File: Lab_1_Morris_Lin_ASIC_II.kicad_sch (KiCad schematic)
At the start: 100 parts, among them IC1 74CBTLV3253D,118, IC2 74CBTLV3253D,118, IC3 74CBTLV3253D,118, IC4 74CBTLV3253D,118, IC5 74CBTLV3253D,118, IC6 74CBTLV3253D,118, J1 VDDPST_External, J10 Conn_01x14, J11 Conn_01x14, J2 PMOD_A, J3 PMOD_B, J4 VDD_Qn External, J5 VDDPST External, J6 PMOD_A, J7 PMOD_B, J8 Conn_01x14, J9 Conn_01x14, Q1 BSS138, U1 TLV75710PDBV, U2 TLV75710PDBV

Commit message: Routing Attempt 2 initial
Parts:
- removed D7: ~{OE}, LED_SMD:LED_1206_3216Metric_Pad1.42x1.75mm_HandSolder, symbol Device:LED
- removed J1: VDDPST_External, Connector:Banana_Jack_2Pin, symbol Connector_Generic:Conn_01x02
- removed R8: 470, Resistor_SMD:R_1206_3216Metric_Pad1.30x1.75mm_HandSolder, symbol Device:R_US
- added J12: VDDPST External, Connector:Banana_Jack_2Pin, symbol Connector_Generic:Conn_01x02
- H1, H2, H3, H4: symbol Mechanical:MountingHole -> Mechanical:MountingHole_Pad
- J2, J3: now in the parts list
- J5: value VDDPST External -> VDDRING External
- J6: value PMOD_A -> Logic_Analyzer_PMOD_A; footprint ASIC_II:PinHeader_VertNum_2x06_P2.54mm_Vertical -> ASIC_II:PinHeader_VertNum_2x05_P2.54mm_Vertical; symbol Connector_Generic:Conn_02x06_Top_Bottom -> Connector_Generic:Conn_02x05_Top_Bottom; now in the parts list
- J7: value PMOD_B -> Logic_Analyzer_PMOD_B; footprint ASIC_II:PinHeader_VertNum_2x06_P2.54mm_Vertical -> ASIC_II:PinHeader_VertNum_2x05_P2.54mm_Vertical; symbol Connector_Generic:Conn_02x06_Top_Bottom -> Connector_Generic:Conn_02x05_Top_Bottom; now in the parts list
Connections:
- net GND: now also J6.10 (Pin_10), J6.5 (Pin_5), J7.10 (Pin_10), J7.5 (Pin_5), J12.2 (Pin_2); no longer J6.12 (Pin_12), J6.6 (Pin_6), J7.12 (Pin_12), J7.6 (Pin_6), JP5.3 (B), JP6.3 (B), JP9.3 (B)
- net PMOD_A10: now also J6.9 (Pin_9); no longer J6.10 (Pin_10)
- net PMOD_A7: now also J6.6 (Pin_6); no longer J6.7 (Pin_7)
- net PMOD_A8: now also J6.7 (Pin_7); no longer J6.8 (Pin_8)
- net PMOD_A9: now also J6.8 (Pin_8); no longer J6.9 (Pin_9)
- net PMOD_B10: now also J7.9 (Pin_9), JP6.3 (B); no longer J7.10 (Pin_10)
- net PMOD_B7: now also J7.6 (Pin_6); no longer J7.7 (Pin_7)
- net PMOD_B8: now also J7.7 (Pin_7), JP5.3 (B); no longer J7.8 (Pin_8)
- net PMOD_B9: now also J7.8 (Pin_8), JP9.3 (B); no longer J7.9 (Pin_9)
- net at JP1.3 (B): now also J12.1 (Pin_1)
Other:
- note removed: "Output Disabled LED"
- moved on the sheet: C6, J10, R10, R5, R6

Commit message: Preroute self planned
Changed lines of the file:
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@@
 		)
 	)
-	(text "Select Lines and ~{OE}\nIndicator LEDs"
+	(text "Select Lines and ~{OE} Indicator LEDs"
 		(exclude_from_sim no)
 		(at 17.78 214.63 0)
@@
 		)
 	)
-	(netclass_flag ""
-		(length 2.54)
-		(shape round)
-		(at 44.45 115.57 0)
-		(fields_autoplaced yes)
-		(effects
-			(font
-				(size 1.27 1.27)
+	(rule_area
+		(exclude_from_sim no)
+		(in_bom yes)
+		(on_board yes)
+		(dnp no)
+		(polyline
+			(pts
+				(xy 16.51 222.25) (xy 16.51 254) (xy 72.39 254) (xy 72.39 222.25)
 			)
-			(justify left bottom)
-		)
-		(property "Netclass" "Power"
-			(at 45.1485 113.03 0)
-			(show_name no)
-			(do_not_autoplace no)
-			(effects
-				(font
-					(size 1.27 1.27)
-				)
-				(justify left)
+			(stroke
+				(width 0)
+				(type dash)
 			)
-		)
-		(property "Component Class" ""
-			(at 62.23 113.03 0)
-			(show_name no)
-			(do_not_autoplace no)
-			(effects
-				(font
-					(size 1.27 1.27)
-					(italic yes)
-				)
+			(fill
+				(type none)
 			)
 		)
 	)
-	(netclass_flag ""
-		(length 2.54)
-		(shape round)
-		(at 69.85 74.93 0)
-		(fields_autoplaced yes)
-		(effects
-			(font
-				(size 1.27 1.27)
+	(rule_area
+		(exclude_from_sim no)
+		(in_bom yes)
+		(on_board yes)
+		(dnp no)
+		(polyline
+			(pts
+				(xy 16.51 16.51) (xy 16.51 138.43) (xy 130.81 138.43) (xy 130.81 16.51)
+			)
+			(stroke
+				(width 0)
+				(type dash)
 			)
-			(justify left bottom)
-		)
-		(property "Netclass" "Power"
-			(at 70.5485 72.39 0)
-			(show_name no)
-			(do_not_autoplace no)
-			(effects
-				(font
-					(size 1.27 1.27)
-				)
-				(justify left)
-			)
-		)
-		(property "Component Class" ""
-			(at 87.63 72.39 0)
-			(show_name no)
-			(do_not_autoplace no)
-			(effects
-				(font
-					(size 1.27 1.27)
-					(italic yes)
-				)
+			(fill
+				(type none)
 			)
 		)
@@
 	(netclass_flag ""
 		(length 2.54)
-		(shape round)
-		(at 60.96 133.35 180)
+		(shape diamond)
+		(at 78.74 16.51 180)
 		(fields_autoplaced yes)
 		(effects
@@
 		)
 		(property "Netclass" "Power"
-			(at 61.6585 135.89 0)
-			(show_name no)
-			(do_not_autoplace no)
-			(effects
-				(font
-					(size 1.27 1.27)
-				)
-				(justify left)
-			)
-		)
-		(property "Component Class" ""
-			(at 78.74 130.81 0)
-			(show_name no)
-			(do_not_autoplace no)
-			(effects
-				(font
-					(size 1.27 1.27)
-					(italic yes)
-				)
-			)
-		)
-	)
-	(netclass_flag ""
-		(length 2.54)
-		(shape round)
-		(at 40.64 25.4 0)
-		(fields_autoplaced yes)
-		(effects
-			(font
-				(size 1.27 1.27)
-			)
-			(justify left bottom)
-		)
-		(property "Netclass" "Power"
-			(at 41.3385 22.86 0)
-			(show_name no)
-			(do_not_autoplace no)
-			(effects
-				(font
-					(size 1.27 1.27)
-				)
-				(justify left)
-			)
-		)
-		(property "Component Class" ""
-			(at 58.42 22.86 0)
-			(show_name no)
-			(do_not_autoplace no)
-			(effects
-				(font
-					(size 1.27 1.27)
-					(italic yes)
-				)
-			)
-		)
-	)
-	(netclass_flag ""
-		(length 2.54)
-		(shape round)
-		(at 44.45 74.93 0)
-		(fields_autoplaced yes)
-		(effects
-			(font
-				(size 1.27 1.27)
-			)
-			(justify left bottom)
-		)
-		(property "Netclass" "Power"
-			(at 45.1485 72.39 0)
+			(at 79.9465 19.05 0)
 			(show_name no)
 			(do_not_autoplace no)
@@
 		)
 		(property "Component Class" ""
-			(at 62.23 72.39 0)
+			(at 113.03 -59.69 0)
 			(show_name no)
 			(do_not_autoplace no)
@@
 	(netclass_flag ""
 		(length 2.54)
-		(shape round)
-		(at 63.5 110.49 0)
+		(shape diamond)
+		(at 21.59 254 180)
 		(fields_autoplaced yes)
 		(effects
@@
 				(size 1.27 1.27)
 			)
-			(justify left bottom)
+			(justify right bottom)
 		)
 		(property "Netclass" "Power"
-			(at 64.1985 107.95 0)
+			(at 22.7965 256.54 0)
 			(show_name no)
 			(do_not_autoplace no)
@@
 		)
 		(property "Component Class" ""
-			(at 45.72 107.95 0)
+			(at 55.88 177.8 0)
 			(show_name no)
 			(do_not_autoplace no)
@@
 					(italic yes)
 				)
-				(justify left)
 			)
 		)

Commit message: Finalized Board for Milestone 2
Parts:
- added C13, C14, C15, C16: 10u, Capacitor_SMD:C_1206_3216Metric_Pad1.33x1.80mm_HandSolder, symbol Device:C_Small
- added D9: ~{OE}, LED_SMD:LED_1206_3216Metric_Pad1.42x1.75mm_HandSolder, symbol Device:LED
- added JP11: Jumper_3_Open, ASIC_II:PinHeader_SP3T_P2.54mm_Vertical, symbol ASIC_II:Jumper_SP43T_Open
- added R39: 470, Resistor_SMD:R_1206_3216Metric_Pad1.30x1.75mm_HandSolder, symbol Device:R_US
- added R8: 10k, Resistor_SMD:R_1206_3216Metric_Pad1.30x1.75mm_HandSolder, symbol Device:R_US
- D5: symbol ASIC_II:PTVS3V3S1UR,115 -> Device:D_Zener
- JP5, JP6, JP9: footprint Connector_PinHeader_2.54mm:PinHeader_1x03_P2.54mm_Vertical -> ASIC_II:PinHeader_SP3T_P2.54mm_Vertical; symbol Jumper:Jumper_3_Open -> ASIC_II:Jumper_SP43T_Open; now in the parts list
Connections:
- net GND: now also JP5.4 (D), JP6.4 (D), JP9.4 (D), C13.2, C14.2, C15.2, C16.2, D9.1 (K), JP11.4 (D)
- net PMOD_B10: now also JP11.3 (C)
- net SEL_b0: now also JP5.1 (A); no longer JP5.2 (C)
- net SEL_b1: now also JP9.1 (A); no longer JP9.2 (C)
- net VDDPST: now also JP5.2 (B), JP6.2 (B), JP9.2 (B), JP11.2 (B), R8.1; no longer JP5.1 (A), JP6.1 (A), JP9.1 (A)
- net VDD_Q1: now also C13.1
- net VDD_Q2: now also C14.1
- net VDD_Q3: now also C15.1
- net VDD_Q4: now also C16.1
- net ~{OE}: now also JP6.1 (A), R39.1; no longer IC4.1 (1~{OE}), JP6.2 (C)
- new net: D9.2 (A), R39.2
- new net ~{CLK_OE}: IC4.1 (1~{OE}), JP11.1 (A), R8.2
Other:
- note added: "OE Disabled LED"
- moved on the sheet: R10, R5, R6

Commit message: Adjusted BOM, Finalized Milestone 2
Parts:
- C1, C2, C3, C4: Mouser Part Number (none) -> 187-CL31B105KAHNFNE
- C10, C11, C12, C6, C7, C8, C9: Mouser Part Number (none) -> 187-CL31B104KBCNFNC
- C13, C14, C15, C16, C5: Mouser Part Number (none) -> 187-CL31A106KAHNNNF
- D1, D2, D3, D4, D6, D8, D9: Mouser Part Number (none) -> 859-LTST-C230KRKT
- R1, R2, R3, R39, R4, R7, R9: Mouser Part Number 660-RK73H2BTTD4700F -> 603-RC1206FR-13470RL
- R10, R11, R12, R13, R14, R15, R16, R17, R18, R19, R20, R21, R22, R23, R24, R25, R26, R27, R28, R29, R30, R31, R32, R33, R34, R35, R36, R37, R38, R5, R6, R8: Mouser Part Number 71-CRCW1206J-10K-E3 -> 603-RC1206JR-0710KP

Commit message: Adjusted footprints to be correct for square header array and SP3T Jumper
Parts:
- J10, J11, J8, J9: footprint Connector_PinHeader_2.54mm:PinHeader_1x14_P2.54mm_Vertical -> ASIC_II:PinHeader_1x14_P2.54mm_Vertical
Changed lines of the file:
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@@
 			)
 		)
-		(property "Footprint" "Connector_PinHeader_2.54mm:PinHeader_1x14_P2.54mm_Vertical"
+		(property "Footprint" "ASIC_II:PinHeader_1x14_P2.54mm_Vertical"
 			(at 204.47 154.94 0)
 			(hide yes)
@@
 			)
 		)
-		(property "Footprint" "Connector_PinHeader_2.54mm:PinHeader_1x14_P2.54mm_Vertical"
+		(property "Footprint" "ASIC_II:PinHeader_1x14_P2.54mm_Vertical"
 			(at 247.65 198.12 0)
 			(hide yes)
@@
 			)
 		)
-		(property "Footprint" "Connector_PinHeader_2.54mm:PinHeader_1x14_P2.54mm_Vertical"
+		(property "Footprint" "ASIC_II:PinHeader_1x14_P2.54mm_Vertical"
 			(at 199.39 238.76 0)
 			(hide yes)
@@
 			)
 		)
-		(property "Footprint" "Connector_PinHeader_2.54mm:PinHeader_1x14_P2.54mm_Vertical"
+		(property "Footprint" "ASIC_II:PinHeader_1x14_P2.54mm_Vertical"
 			(at 154.94 195.58 0)
 			(hide yes)

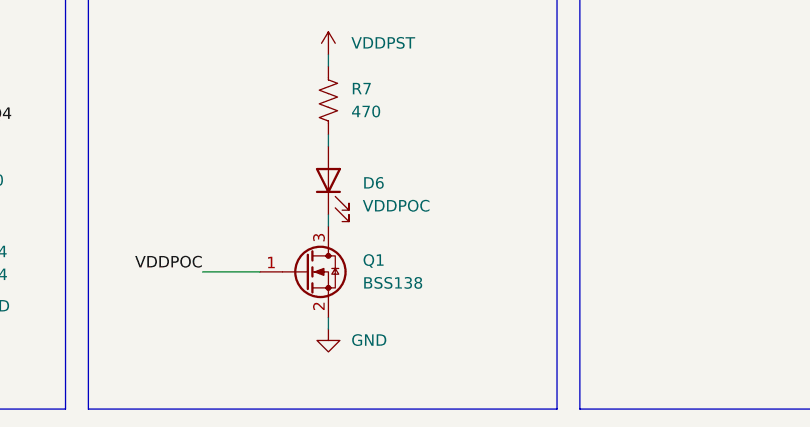
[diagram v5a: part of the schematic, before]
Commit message: Updated bom for availability
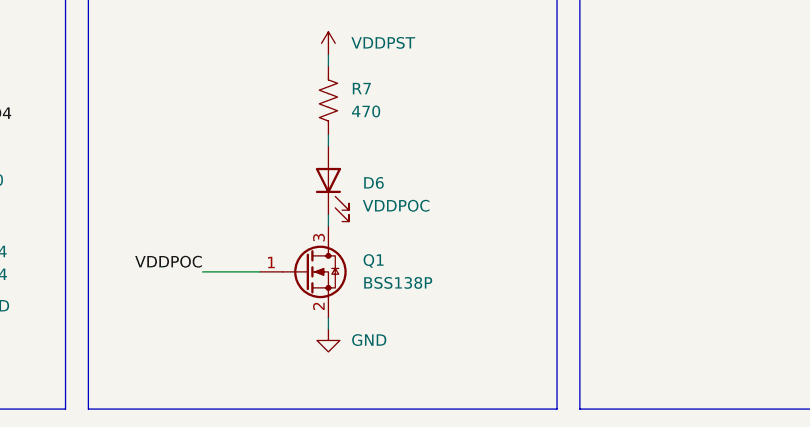
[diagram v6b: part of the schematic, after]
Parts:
- J2, J3: Mouser Part Number (none) -> 649-1012938291203BLF
- Q1: value BSS138 -> BSS138P; Mouser Part Number 771-BSS138AK-QR -> 771-BSS138P215
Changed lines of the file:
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@@
 			)
 		)
+		(property "Mouser Part Number" "649-1012938291203BLF"
+			(at 45.72 158.75 0)
+			(hide yes)
+			(show_name no)
+			(do_not_autoplace no)
+			(effects
+				(font
+					(size 1.27 1.27)
+				)
+			)
+		)
 		(pin "10"
 		)
@@
 			)
 		)
-		(property "Value" "BSS138"
+		(property "Value" "BSS138P"
 			(at 110.49 247.6499 0)
 			(show_name no)
@@
 			)
 		)
-		(property "Datasheet" "https://www.onsemi.com/pub/Collateral/BSS138-D.PDF"
+		(property "Datasheet" "https://assets.nexperia.com/documents/data-sheet/BSS138P.pdf"
 			(at 109.22 250.19 0)
 			(hide yes)
@@
 			)
 		)
-		(property "Mouser Part Number" "771-BSS138AK-QR"
+		(property "Mouser Part Number" "771-BSS138P215"
 			(at 104.14 246.38 0)
 			(hide yes)
@@
 			(at 45.72 189.23 0)
 			(hide yes)
+			(show_name no)
+			(do_not_autoplace no)
+			(effects
+				(font
+					(size 1.27 1.27)
+				)
+			)
+		)
+		(property "Mouser Part Number" "649-1012938291203BLF"
+			(at 45.72 189.23 0)
+			(hide yes)

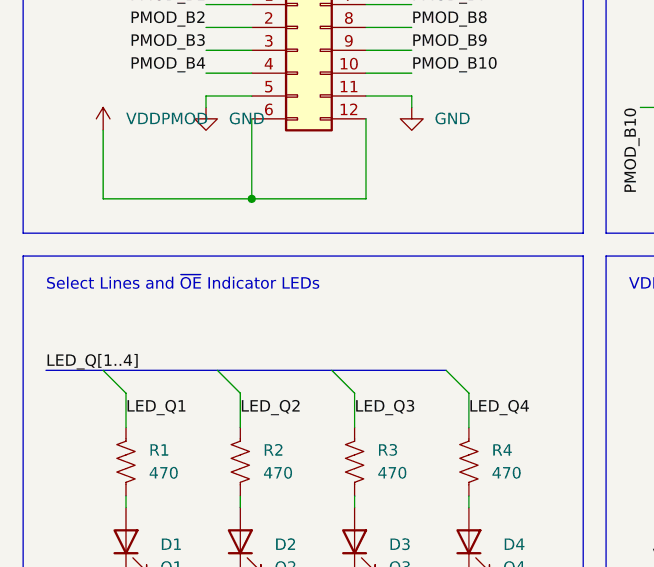
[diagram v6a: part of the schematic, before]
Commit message: Silkscreen for LED labels
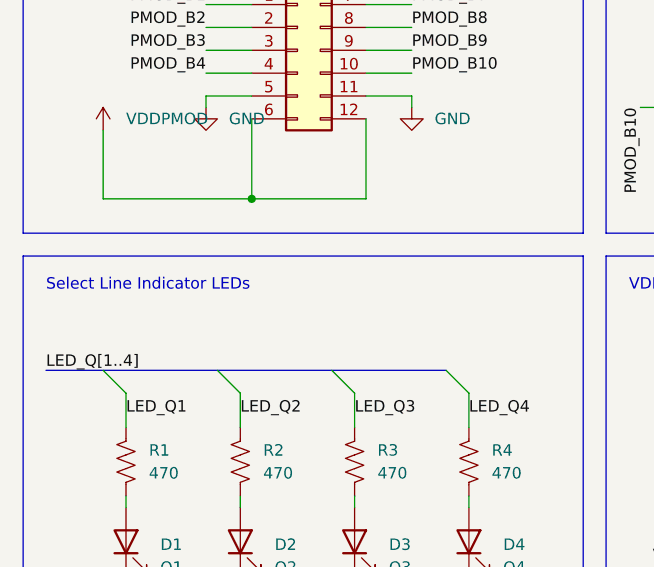
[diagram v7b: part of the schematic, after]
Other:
- note added: "Select Line Indicator LEDs"
- note removed: "Select Lines and ~{OE} Indicator LEDs"
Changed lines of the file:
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@@
 		)
 	)
-	(text "Select Lines and ~{OE} Indicator LEDs"
+	(text "Select Line Indicator LEDs"
 		(exclude_from_sim no)
 		(at 17.78 214.63 0)
